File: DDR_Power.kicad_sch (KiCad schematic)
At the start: 2 parts, among them U4 W634GU6QB

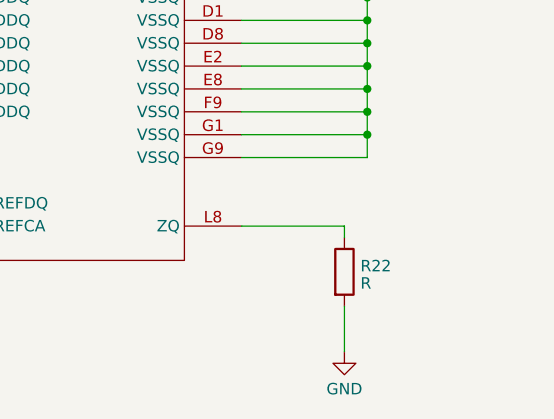
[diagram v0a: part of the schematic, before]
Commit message: updated DDR Power
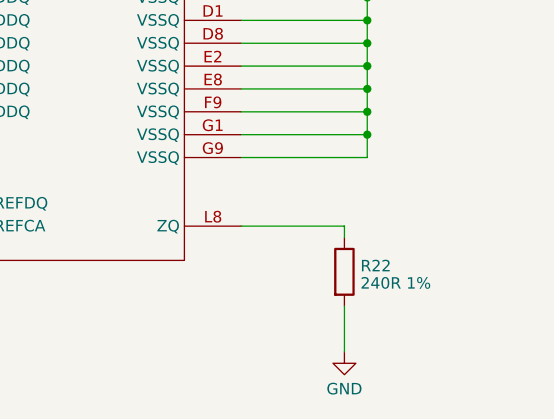
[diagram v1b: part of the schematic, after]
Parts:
- R22: value R -> 240R 1%; footprint (none) -> Resistor_SMD:R_0402_1005Metric
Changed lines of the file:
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@@
       (effects (font (size 1.27 1.27)) (justify left))
     )
-    (property "Value" "R" (at 179.578 115.5773 0)
+    (property "Value" "240R 1%" (at 179.578 115.5773 0)
       (effects (font (size 1.27 1.27)) (justify left))
     )
-    (property "Footprint" "" (at 176.022 114.3 90)
+    (property "Footprint" "Resistor_SMD:R_0402_1005Metric" (at 176.022 114.3 90)
       (effects (font (size 1.27 1.27)) hide)
     )

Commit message: updated DDR
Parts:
- added C49, C50, C51, C52, C53, C55, C56, C57: 1nF X7R 50V, Capacitor_SMD:C_0402_1005Metric, symbol Device:C
- added R23, R24: 10K 1%, Resistor_SMD:R_0402_1005Metric, symbol Device:R
- added R25, R26: 0R 5%, Resistor_SMD:R_0402_1005Metric, symbol Device:R
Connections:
- net GND: now also C50.2, C51.2, C52.2, C53.2, C55.2, C56.2, R24.2
- net VCC_DDR: now also C49.1, C57.1, R23.1
- net DDR_VREFDQ: now reaches U4.H1 (VREFDQ)
- net DDR_VREFDQ: now also C55.1, C56.1, C57.2, R25.2, R26.1
- net DDR_VREFCA: now reaches U4.M8 (VREFCA)
- net DDR_VREFCA: now also C49.2, C50.1, C51.1, C52.1, C53.1, R25.1
- new net: R23.2, R24.1
- new net DDR_VREF: R26.2
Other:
- added sheet DDR Filter Capacitors (DDR_filter_capacitors.kicad_sch)
- note added: "Close to DDR"
- note added: "DNP"
- moved on the sheet: R22, U4B

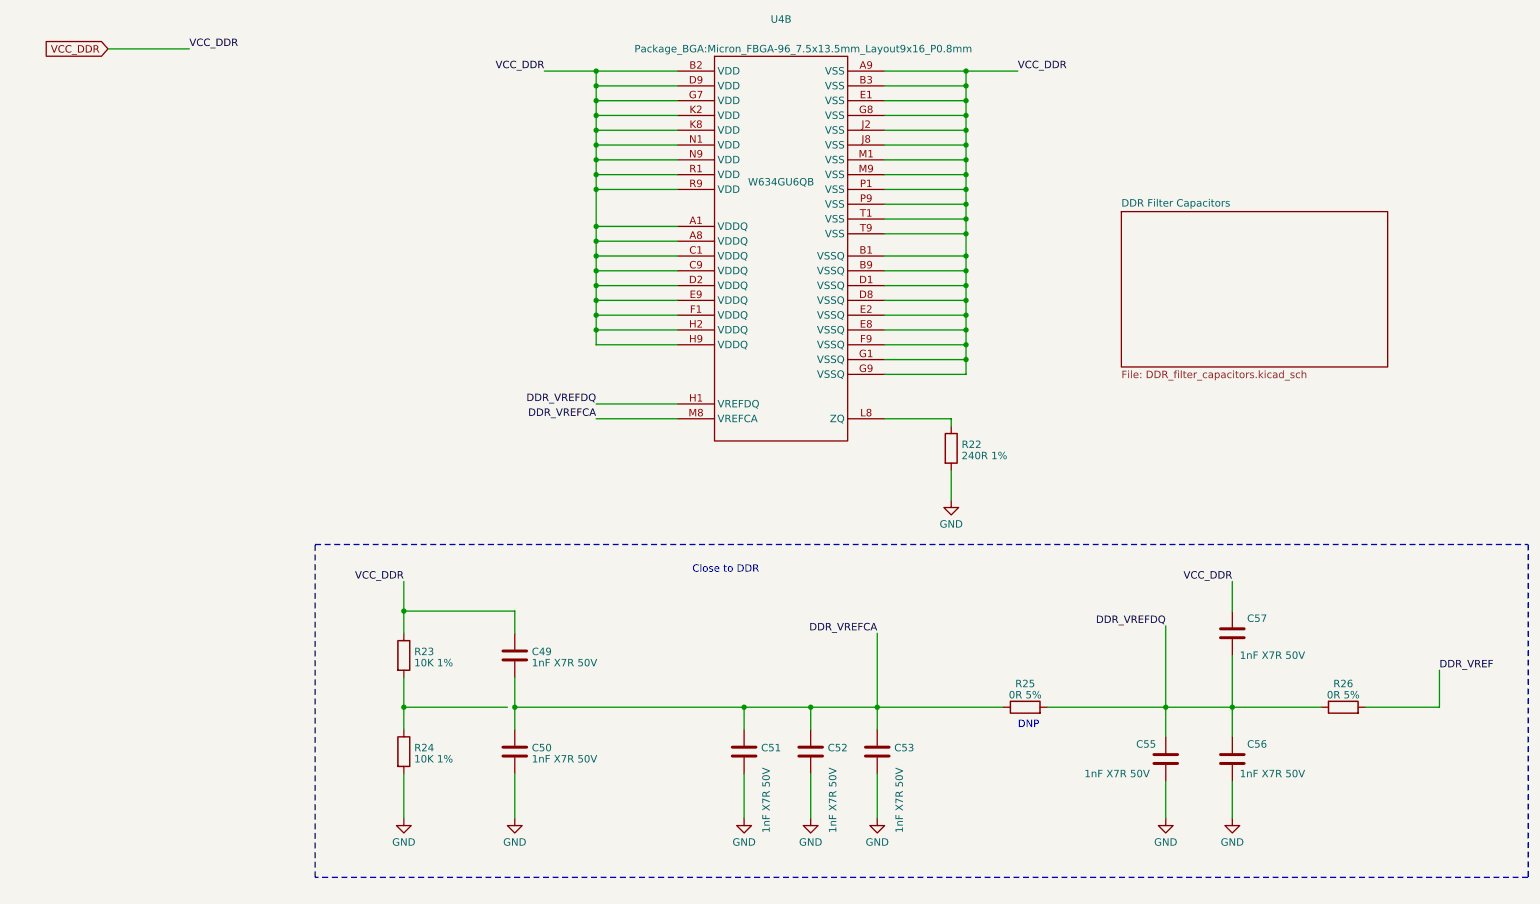
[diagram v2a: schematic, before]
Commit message: replace DDR3 with DDR4
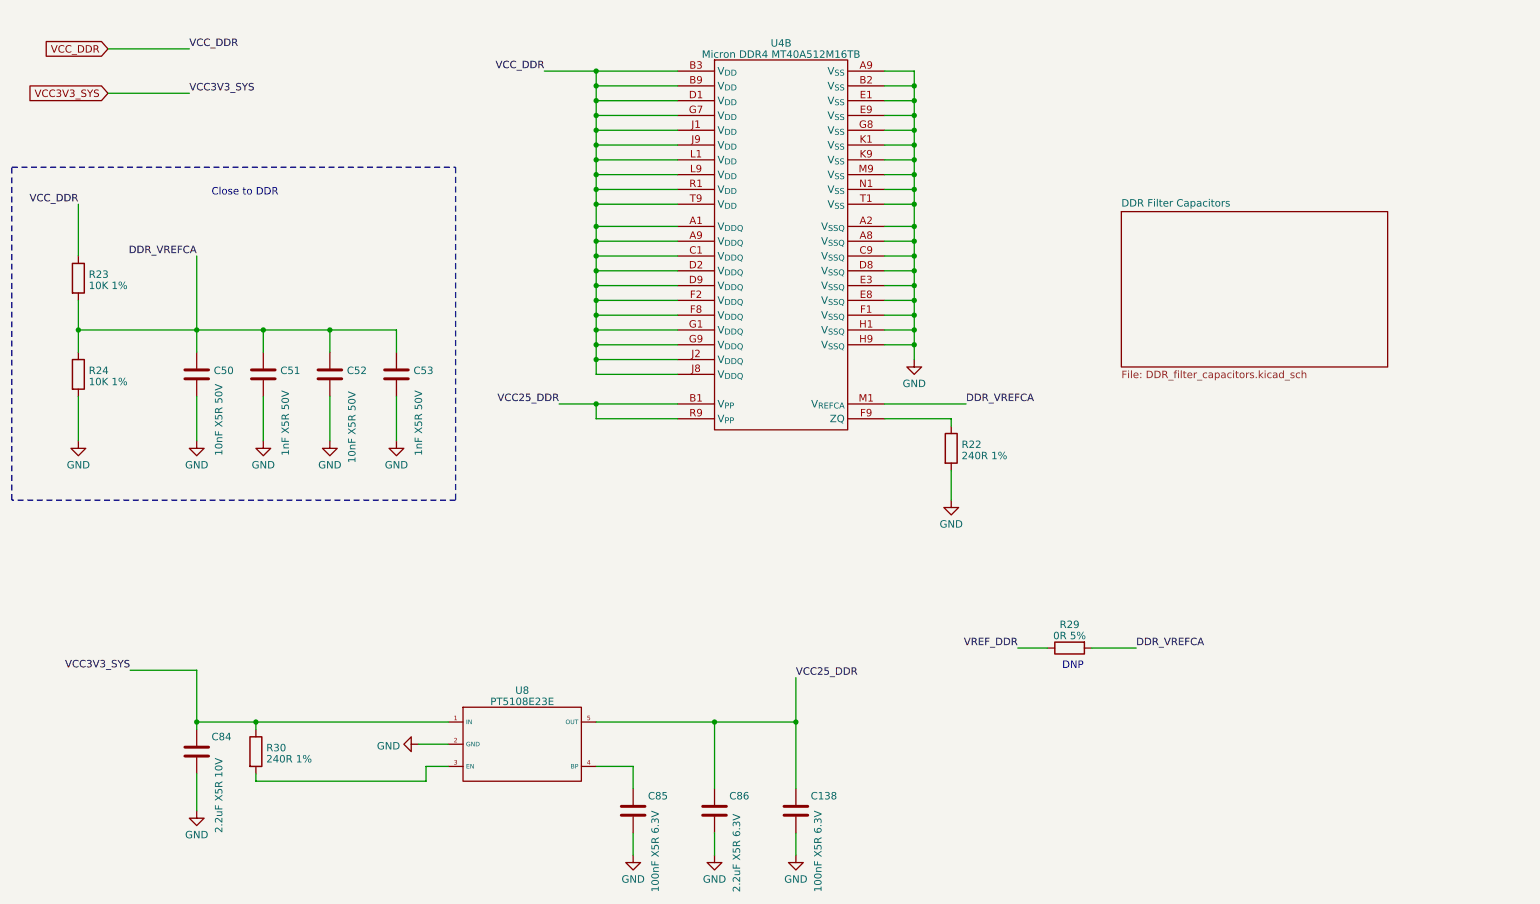
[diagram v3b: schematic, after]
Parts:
- removed C49, C55, C56, C57: 1nF X7R 50V, Capacitor_SMD:C_0402_1005Metric, symbol Device:C
- removed R25, R26: 0R 5%, Resistor_SMD:R_0402_1005Metric, symbol Device:R
- removed U4: W634GU6QB, Package_BGA:Micron_FBGA-96_7.5x13.5mm_Layout9x16_P0.8mm, symbol Memory_DDR:W634GU6QB
- added C138, C85: 100nF X5R 6.3V, Capacitor_SMD:C_0402_1005Metric, symbol Device:C
- added C84: 2.2uF X5R 10V, Capacitor_SMD:C_0402_1005Metric, symbol Device:C
- added C86: 2.2uF X5R 6.3V, Capacitor_SMD:C_0402_1005Metric, symbol Device:C
- added R29: 0R 5%, Resistor_SMD:R_0402_1005Metric, symbol Device:R
- added R30: 240R 1%, Resistor_SMD:R_0402_1005Metric, symbol Device:R
- added U4: Micron DDR4 MT40A512M16TB, symbol Memory_DDR:Micron_DDR4_MT40A512M16TB
- added U8: PT5108E23E, Package_TO_SOT_SMD:SOT-23-5, symbol Leaf_Converter_DCDC:PT5108E23E
- C50, C52: value 1nF X7R 50V -> 10nF X5R 50V
- C51, C53: value 1nF X7R 50V -> 1nF X5R 50V
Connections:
- net DDR_VREFCA: now also R23.2, R24.1, R29.2, U4.M1 (V_{REFCA})
- net GND: now also C138.2, C84.2, C85.2, C86.2, U4.A2 (V_{SSQ}), U4.A8 (V_{SSQ}), U4.A9 (V_{SS}), U4.B2 (V_{SS}), U4.C9 (V_{SSQ}), U4.D8 (V_{SSQ}), U4.E1 (V_{SS}), U4.E3 (V_{SSQ}), U4.E8 (V_{SSQ}), U4.E9 (V_{SS}), U4.F1 (V_{SSQ}), U4.G8 (V_{SS}), U4.H1 (V_{SSQ}), U4.H9 (V_{SSQ}), U4.K1 (V_{SS}), U4.K9 (V_{SS}), U4.M9 (V_{SS}), U4.N1 (V_{SS}), U4.T1 (V_{SS}), U8.2 (GND)
- net VCC_DDR: now also U4.A1 (V_{DDQ}), U4.A9 (V_{SS}), U4.B3 (V_{DD}), U4.B9 (V_{DD}), U4.C1 (V_{DDQ}), U4.D1 (V_{DD}), U4.D2 (V_{DDQ}), U4.D9 (V_{DDQ}), U4.F2 (V_{DDQ}), U4.F8 (V_{DDQ}), U4.G1 (V_{DDQ}), U4.G7 (V_{DD}), U4.G9 (V_{DDQ}), U4.J1 (V_{DD}), U4.J2 (V_{DDQ}), U4.J8 (V_{DDQ}), U4.J9 (V_{DD}), U4.L1 (V_{DD}), U4.L9 (V_{DD}), U4.R1 (V_{DD}), U4.T9 (V_{DD})
- net at R22.1: now also U4.F9 (ZQ)
- new net: R30.2, U8.3 (EN)
- new net: C85.1, U8.4 (BP)
- new net VCC25_DDR: C138.1, C86.1, U4.B1 (V_{PP}), U4.R9 (V_{PP}), U8.5 (OUT)
- new net VCC3V3_SYS: C84.1, R30.1, U8.1 (IN)
- new net VREF_DDR: R29.1
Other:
- moved on the sheet: C50, C51, C52, C53, R23, R24

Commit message: updated footprints
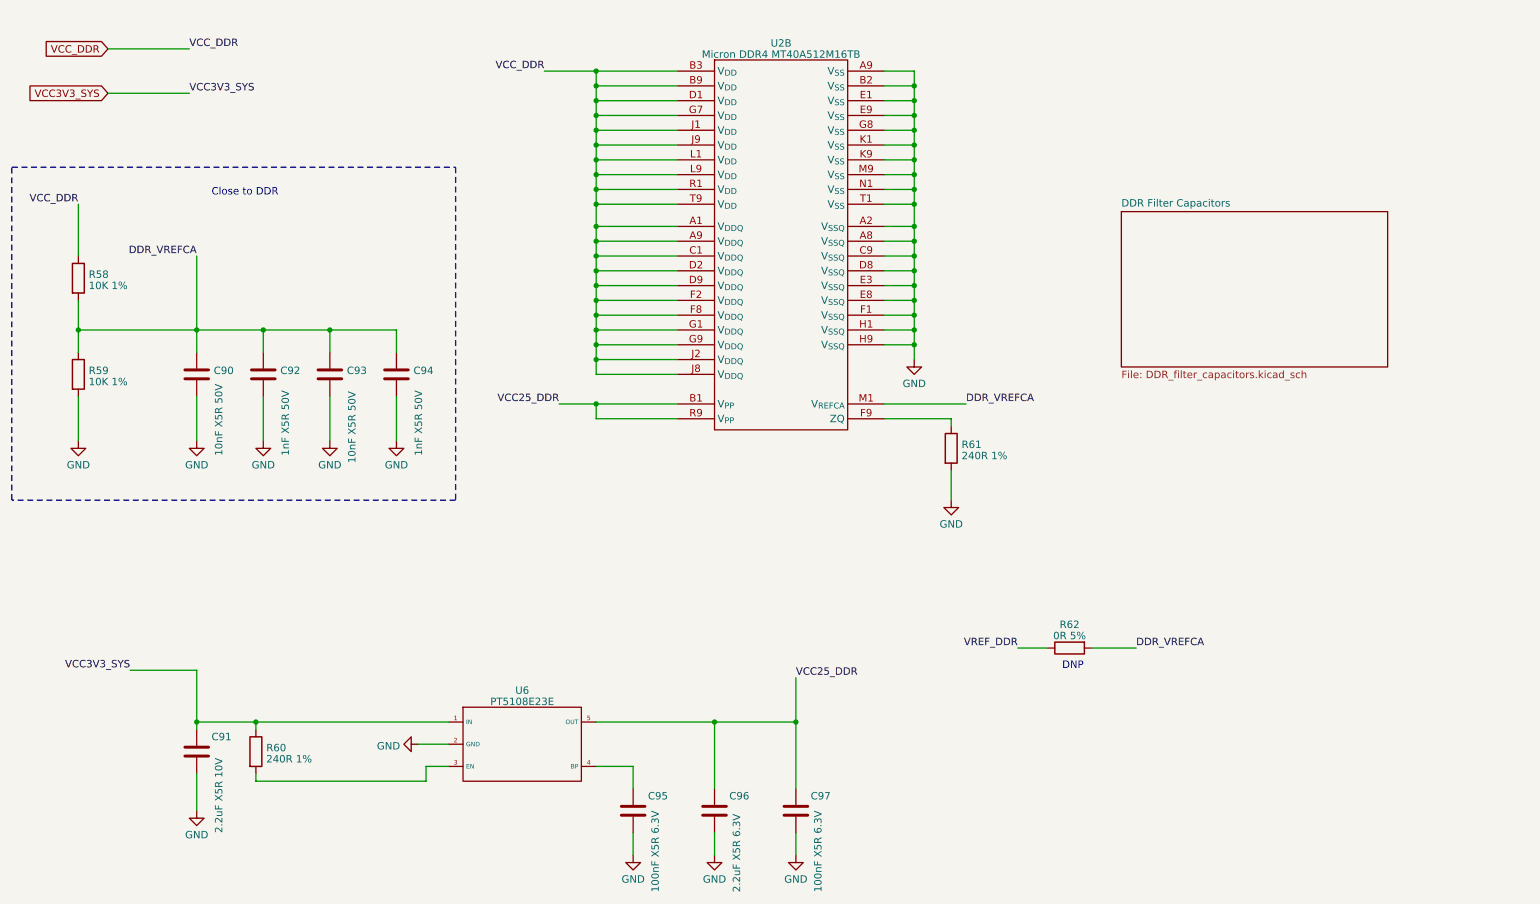
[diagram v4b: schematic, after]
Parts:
- U2: renamed from U4; footprint (none) -> Package_BGA:Micron_FBGA-96_9x14mm_Layout9x16_P0.8mm
- renumbered C50 to C90, C84 to C91, C51 to C92, C52 to C93, C53 to C94, C85 to C95, C86 to C96, C138 to C97, R23 to R58, R24 to R59, R30 to R60, R22 to R61, R29 to R62, U8 to U6

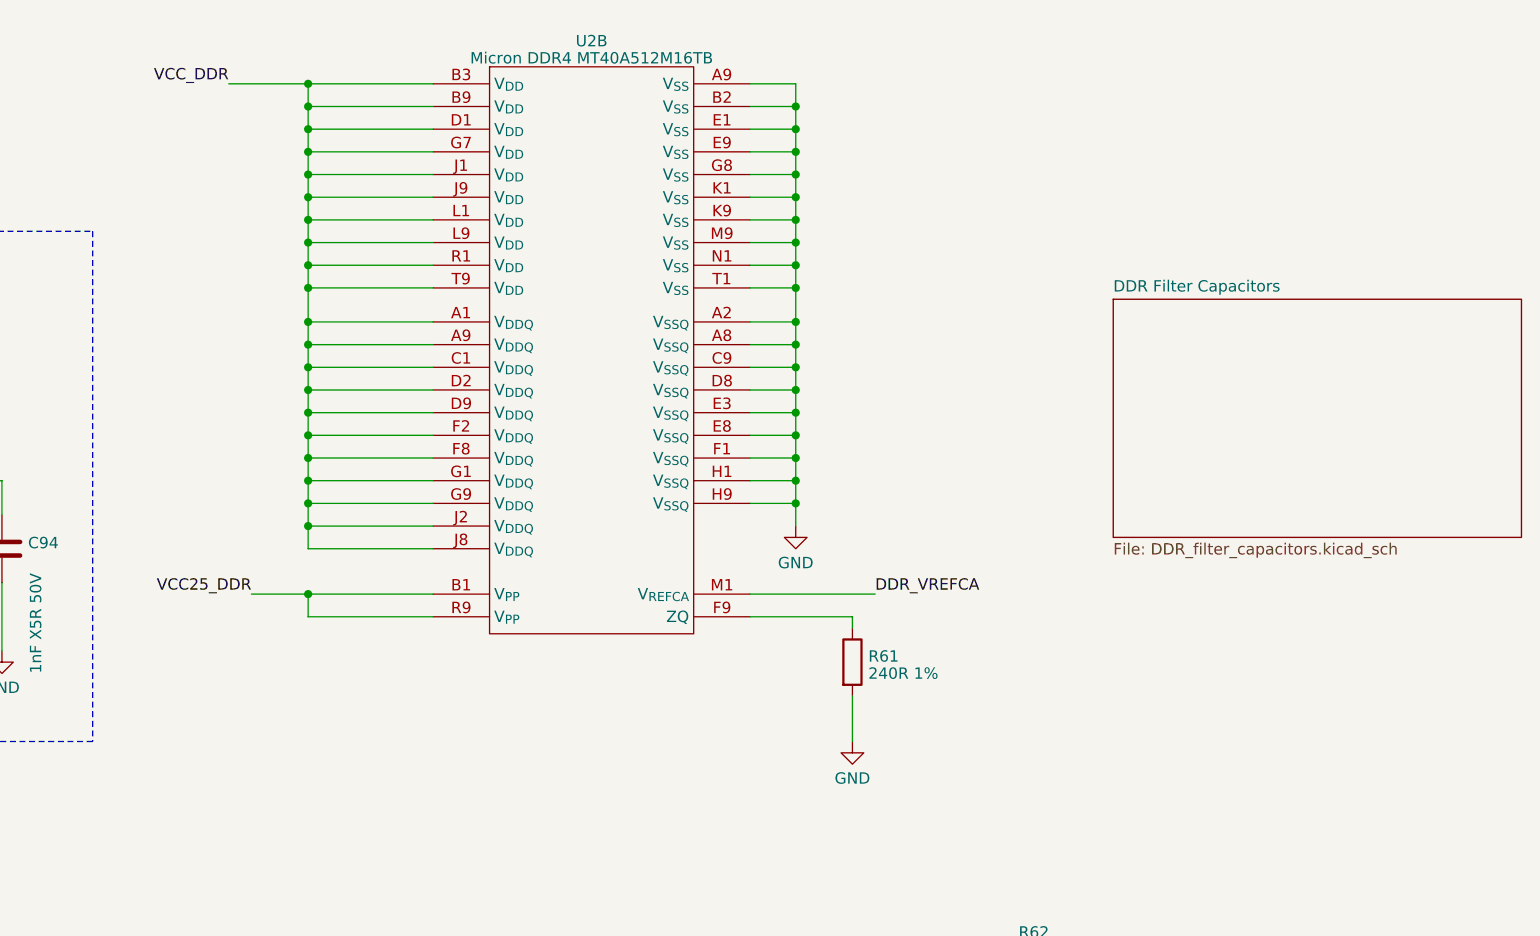
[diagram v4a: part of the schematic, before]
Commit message: updated Capacitors
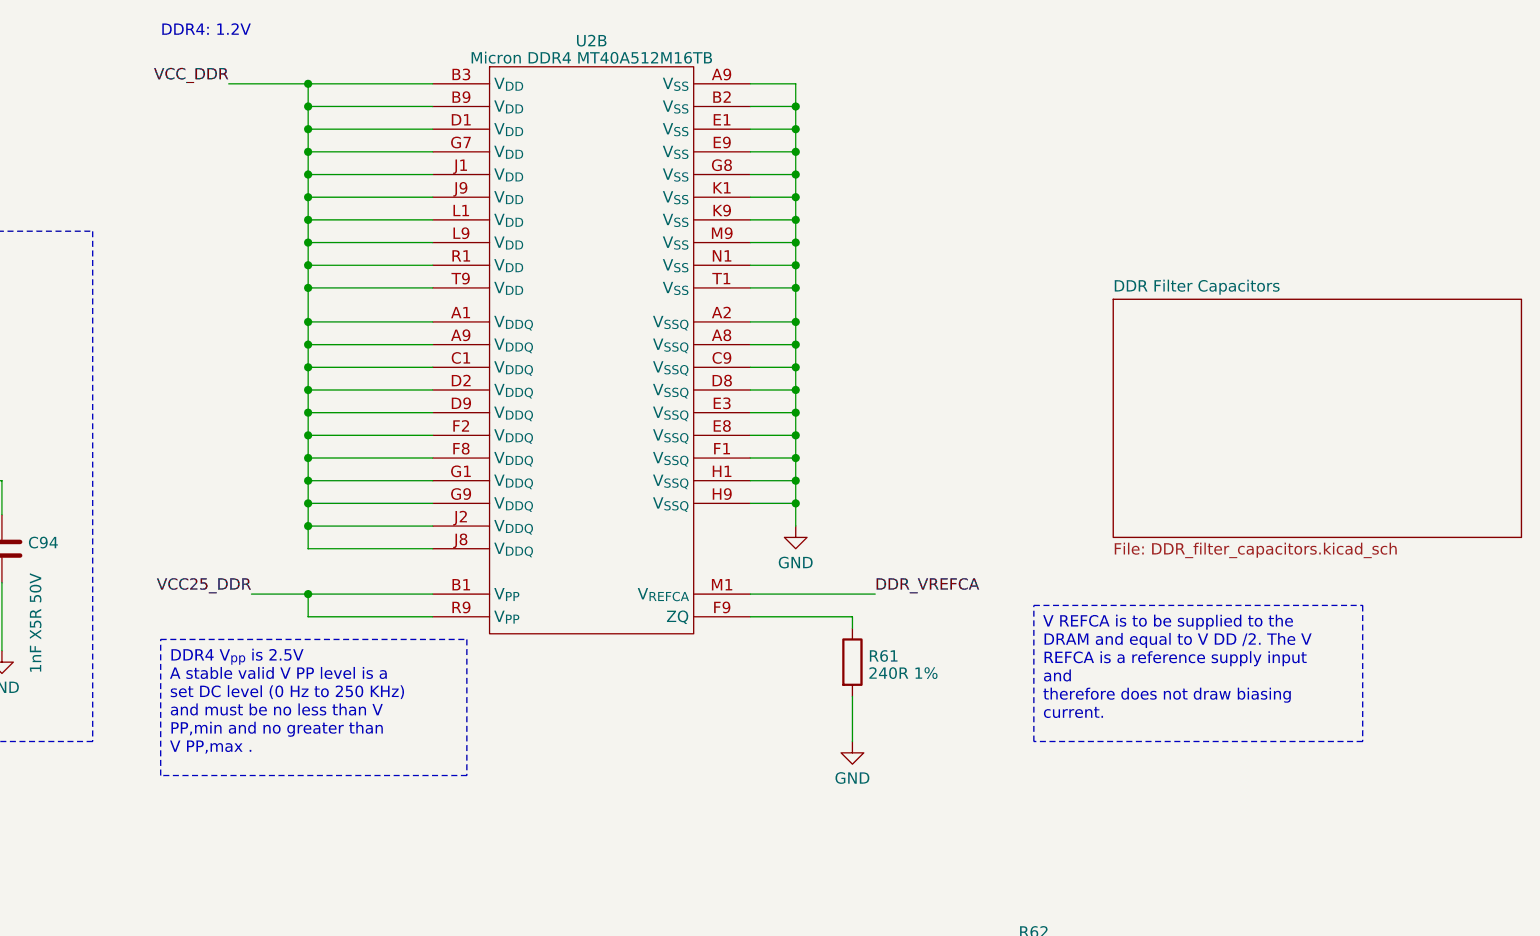
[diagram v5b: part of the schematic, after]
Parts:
- C95, C97: footprint Capacitor_SMD:C_0402_1005Metric -> Capacitor_SMD:C_0201_0603Metric; LCSC (none) -> C76934; Model (none) -> GRM033R61A104KE15D; Vendor (none) -> muRata(村田)
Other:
- note added: "DDR4: 1.2V"
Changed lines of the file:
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@@
     (fill (type none))
+  )
+  (text_box "V REFCA is to be supplied to the DRAM and equal to V DD /2. The V REFCA is a reference supply input and\ntherefore does not draw biasing current."
+    (at 196.85 83.82 0) (size 36.83 15.24)
+    (stroke (width 0) (type dash_dot))
+    (fill (type none))
+    (effects (font (size 1.27 1.27)) (justify left top))
+  )
+  (text_box "DDR4 V_{pp} is 2.5V\nA stable valid V PP level is a set DC level (0 Hz to 250 KHz) and must be no less than V PP,min and no greater than\nV PP,max ."
+    (at 99.06 87.63 0) (size 34.29 15.24)
+    (stroke (width 0) (type dash_dot))
+    (fill (type none))
+    (effects (font (size 1.27 1.27)) (justify left top))
   )
   (text "Close to DDR" (at 49.53 46.99 0)
@@
   (text "DNP" (at 195.58 128.27 0)
     (effects (font (size 1.27 1.27) (color 194 194 0 1)) (justify left bottom))
+  )
+  (text "DDR4: 1.2V" (at 99.06 20.32 0)
+    (effects (font (size 1.27 1.27)) (justify left bottom))
   )
   (label "VCC_DDR" (at 26.67 48.26 180) (fields_autoplaced)
@@
       (effects (font (size 1.27 1.27)) (justify left))
     )
-    (property "Footprint" "Capacitor_SMD:C_0402_1005Metric" (at 150.8252 156.21 0)
+    (property "Footprint" "Capacitor_SMD:C_0201_0603Metric" (at 150.8252 156.21 0)
       (effects (font (size 1.27 1.27)) hide)
     )
     (property "Datasheet" "~" (at 149.86 152.4 0)
+      (effects (font (size 1.27 1.27)) hide)
+    )
+    (property "Description" "容值: 100nF 精度: ±10% 额定电压: 10V 材质(温度系数): X5R 材质:X5R" (at 149.86 152.4 0)
+      (effects (font (size 1.27 1.27)) hide)
+    )
+    (property "LCSC" "C76934" (at 149.86 152.4 0)
+      (effects (font (size 1.27 1.27)) hide)
+    )
+    (property "Model" "GRM033R61A104KE15D" (at 149.86 152.4 0)
+      (effects (font (size 1.27 1.27)) hide)
+    )
+    (property "Vendor" "muRata(村田)" (at 149.86 152.4 0)
       (effects (font (size 1.27 1.27)) hide)
     )
@@
       (effects (font (size 1.27 1.27)) (justify left))
     )
-    (property "Footprint" "Capacitor_SMD:C_0402_1005Metric" (at 122.8852 156.21 0)
+    (property "Footprint" "Capacitor_SMD:C_0201_0603Metric" (at 122.8852 156.21 0)
       (effects (font (size 1.27 1.27)) hide)
     )
@@
       (effects (font (size 1.27 1.27)) hide)
     )
+    (property "Description" "容值: 100nF 精度: ±10% 额定电压: 10V 材质(温度系数): X5R 材质:X5R" (at 121.92 152.4 0)
+      (effects (font (size 1.27 1.27)) hide)
+    )
+    (property "LCSC" "C76934" (at 121.92 152.4 0)
+      (effects (font (size 1.27 1.27)) hide)
+    )
+    (property "Model" "GRM033R61A104KE15D" (at 121.92 152.4 0)
+      (effects (font (size 1.27 1.27)) hide)
+    )
+    (property "Vendor" "muRata(村田)" (at 121.92 152.4 0)
+      (effects (font (size 1.27 1.27)) hide)
+    )
